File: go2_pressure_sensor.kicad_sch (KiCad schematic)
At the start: 11 parts, among them J1 Conn_01x03_Socket, U2 LP2980-ADJ

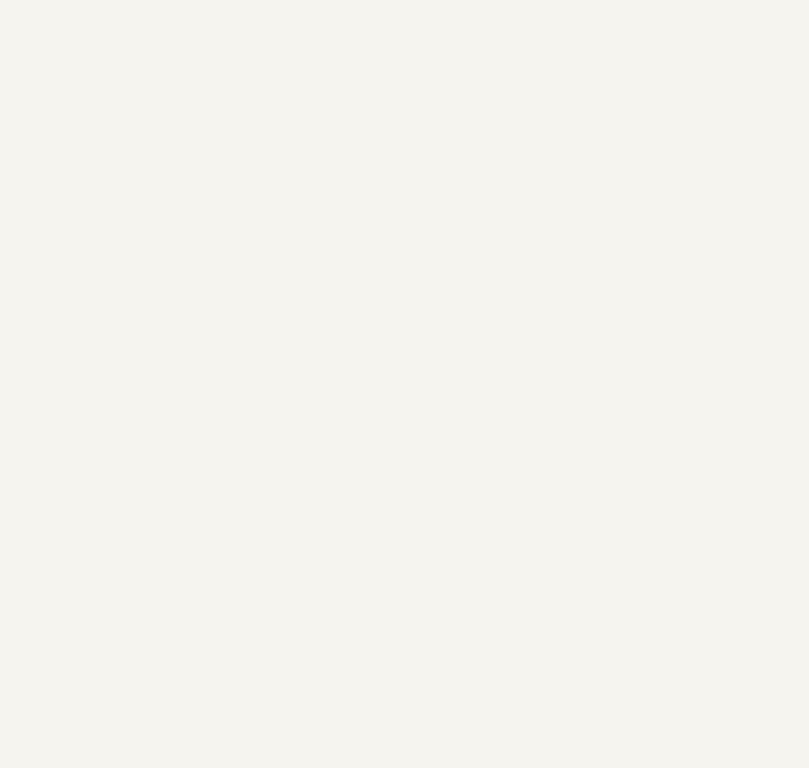
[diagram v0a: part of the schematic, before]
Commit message: Added connector diagram of the GO2 battery (unrelated)
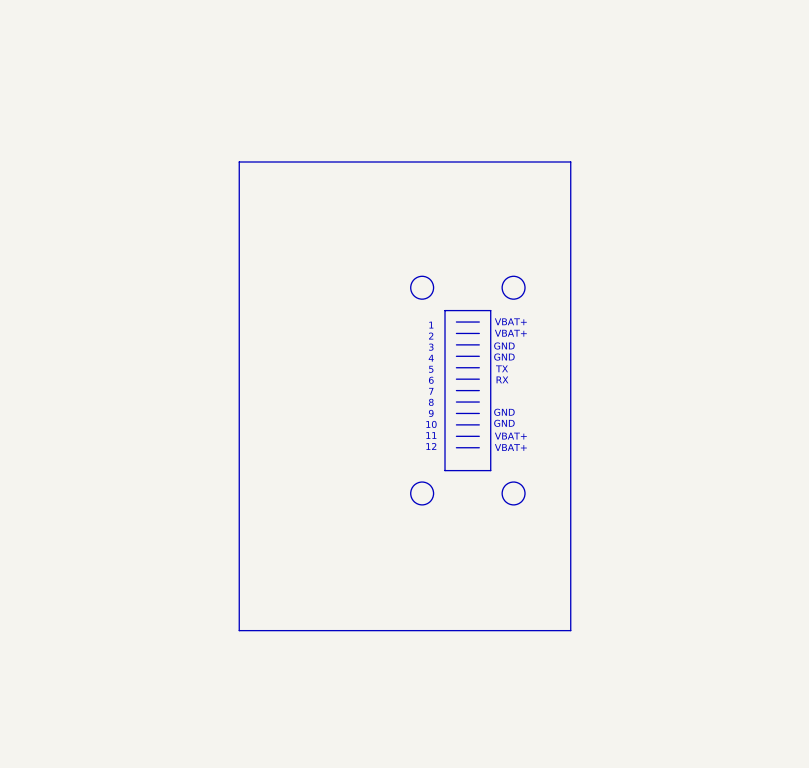
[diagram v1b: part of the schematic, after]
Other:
- note added: "1 2 3 4 5 6 7 8 9 10 11 12"
- note added: "GND GND"
- note added: "TX RX"
- note added: "VBAT+"

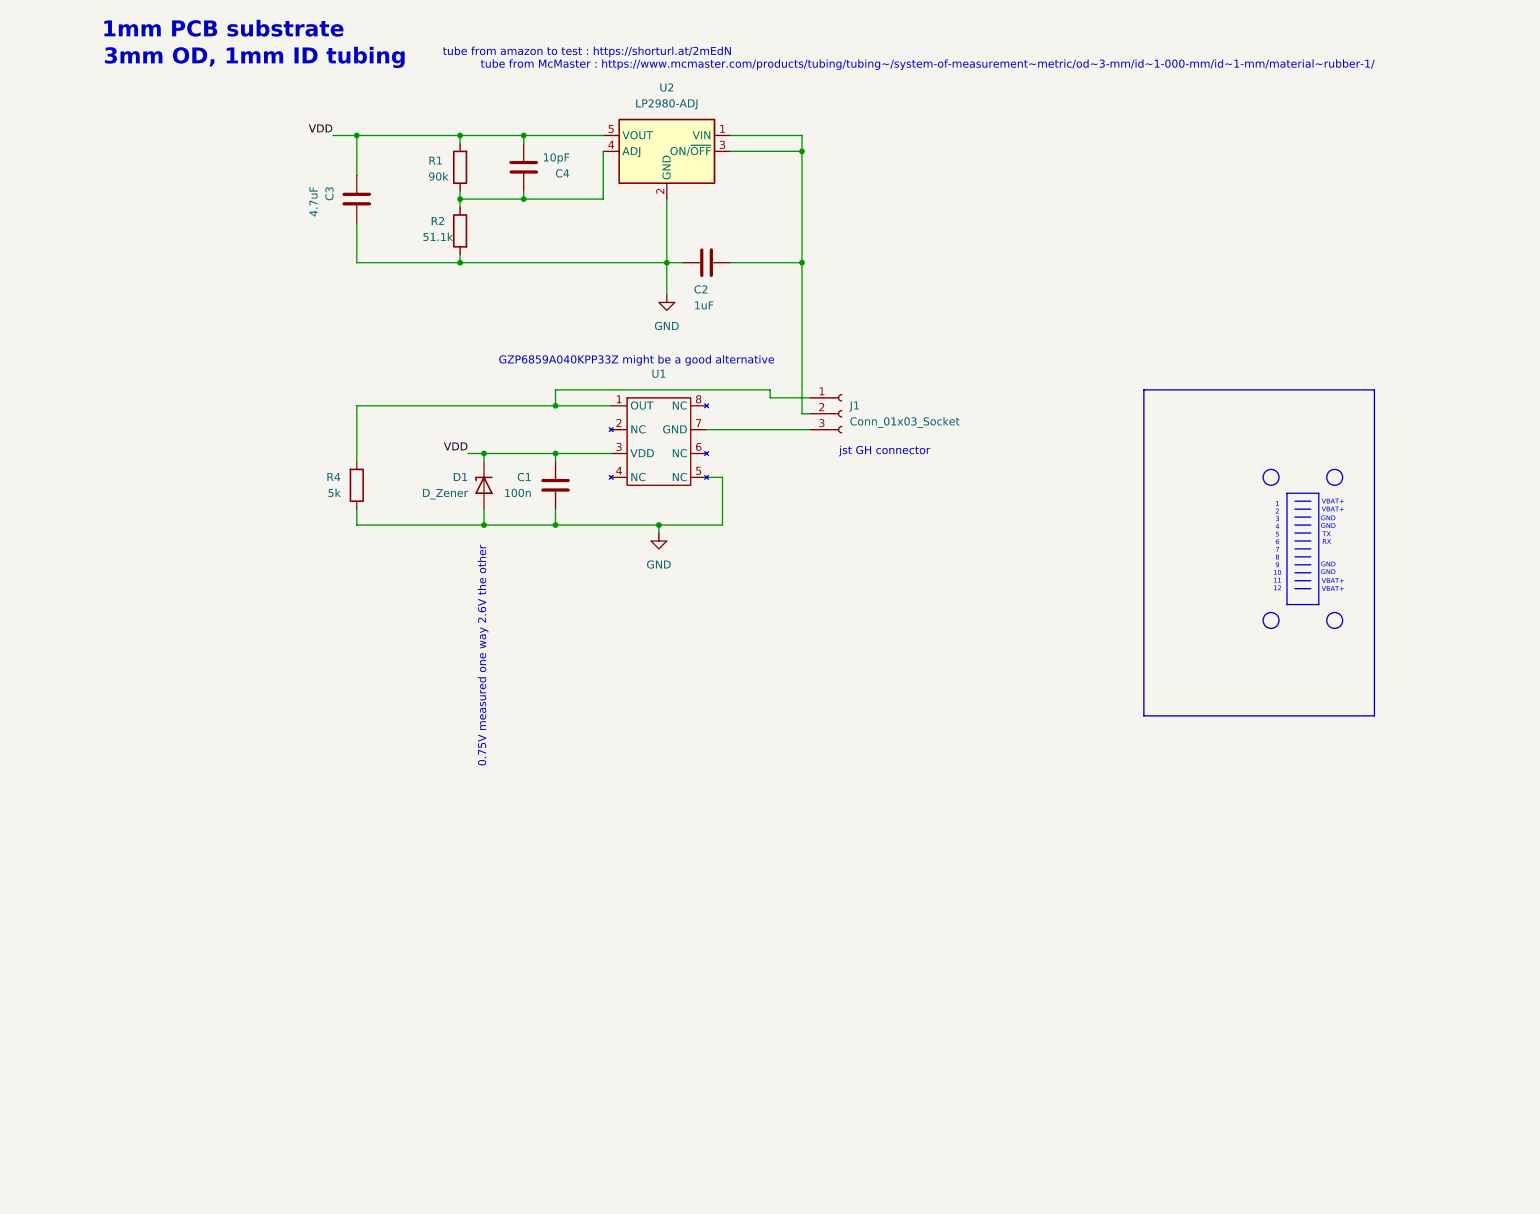
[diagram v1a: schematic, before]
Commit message: Non verified version with new presure transducer
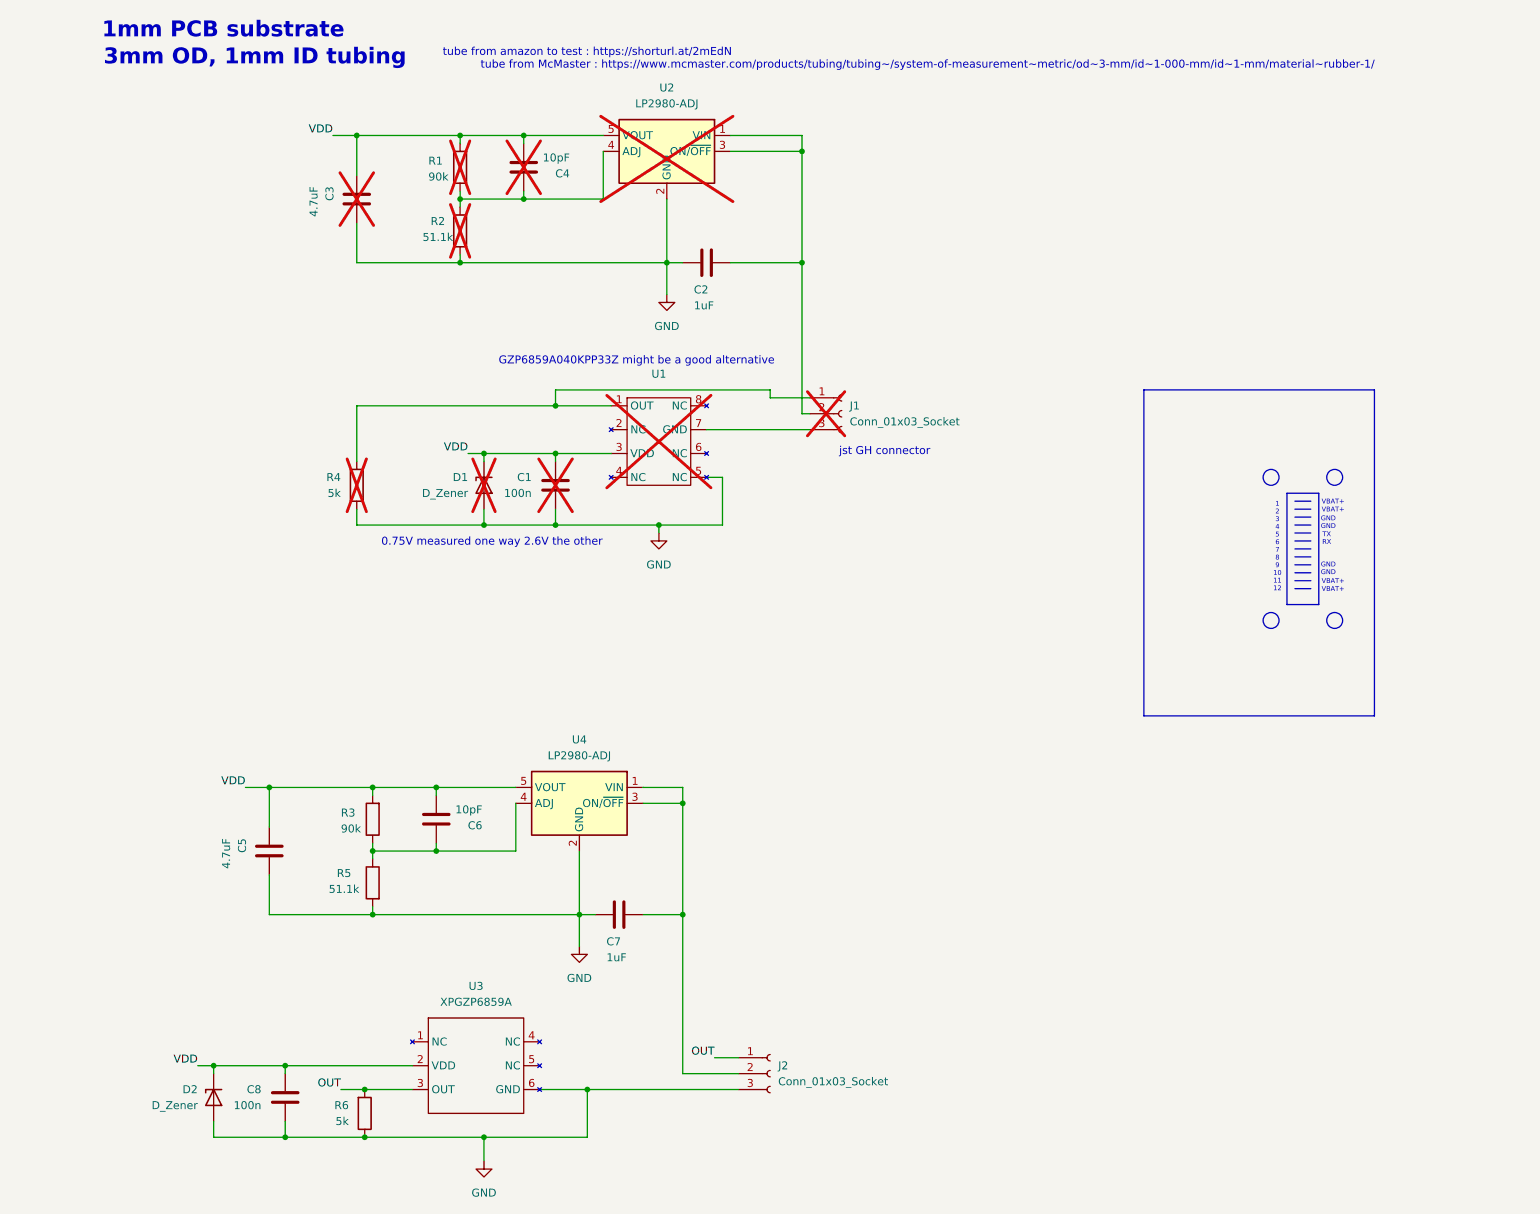
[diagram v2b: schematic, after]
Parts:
- added C5: 4.7uF, Resistor_SMD:R_0603_1608Metric, symbol Device:C
- added C6: 10pF, Resistor_SMD:R_0603_1608Metric, symbol Device:C
- added C7: 1uF, Resistor_SMD:R_0603_1608Metric, symbol Device:C
- added C8: 100n, Resistor_SMD:R_0603_1608Metric, symbol Device:C
- added D2: D_Zener, Diode_SMD:D_0603_1608Metric, symbol Device:D_Zener
- added J2: Conn_01x03_Socket, Connector_JST:JST_GH_BM03B-GHS-TBT_1x03-1MP_P1.25mm_Vertical, symbol Connector:Conn_01x03_Socket
- added R3: 90k, Resistor_SMD:R_0603_1608Metric, symbol Device:R
- added R5: 51.1k, Resistor_SMD:R_0603_1608Metric, symbol Device:R
- added R6: 5k, Resistor_SMD:R_0603_1608Metric, symbol Device:R
- added U3: XPGZP6859A, Ensmasteel_librairy:XGZ6859 6pin, symbol ENSMASTEEL_librairy:XPGZP6859A
- added U4: LP2980-ADJ, Package_TO_SOT_SMD:SOT-23-5, symbol Regulator_Linear:LP2980-ADJ
- C1, C3, C4, D1, J1, R1, R2, R4, U1, U2: now not fitted; now left out of the parts list
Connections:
- net GND: now also C5.1, C7.2, C8.2, D2.2 (A), J2.3 (Pin_3), R5.2, R6.1, U3.6 (GND), U4.2 (GND)
- net VDD: now also C5.2, C6.1, C8.1, D2.1 (K), R3.2, U3.2 (VDD), U4.5 (VOUT)
- new net: C6.2, R3.1, R5.1, U4.4 (ADJ)
- new net: C7.1, J2.2 (Pin_2), U4.1 (VIN), U4.3 (ON/~{OFF})
- new net OUT: J2.1 (Pin_1), R6.2, U3.3 (OUT)

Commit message: Removed copied sensors schematic
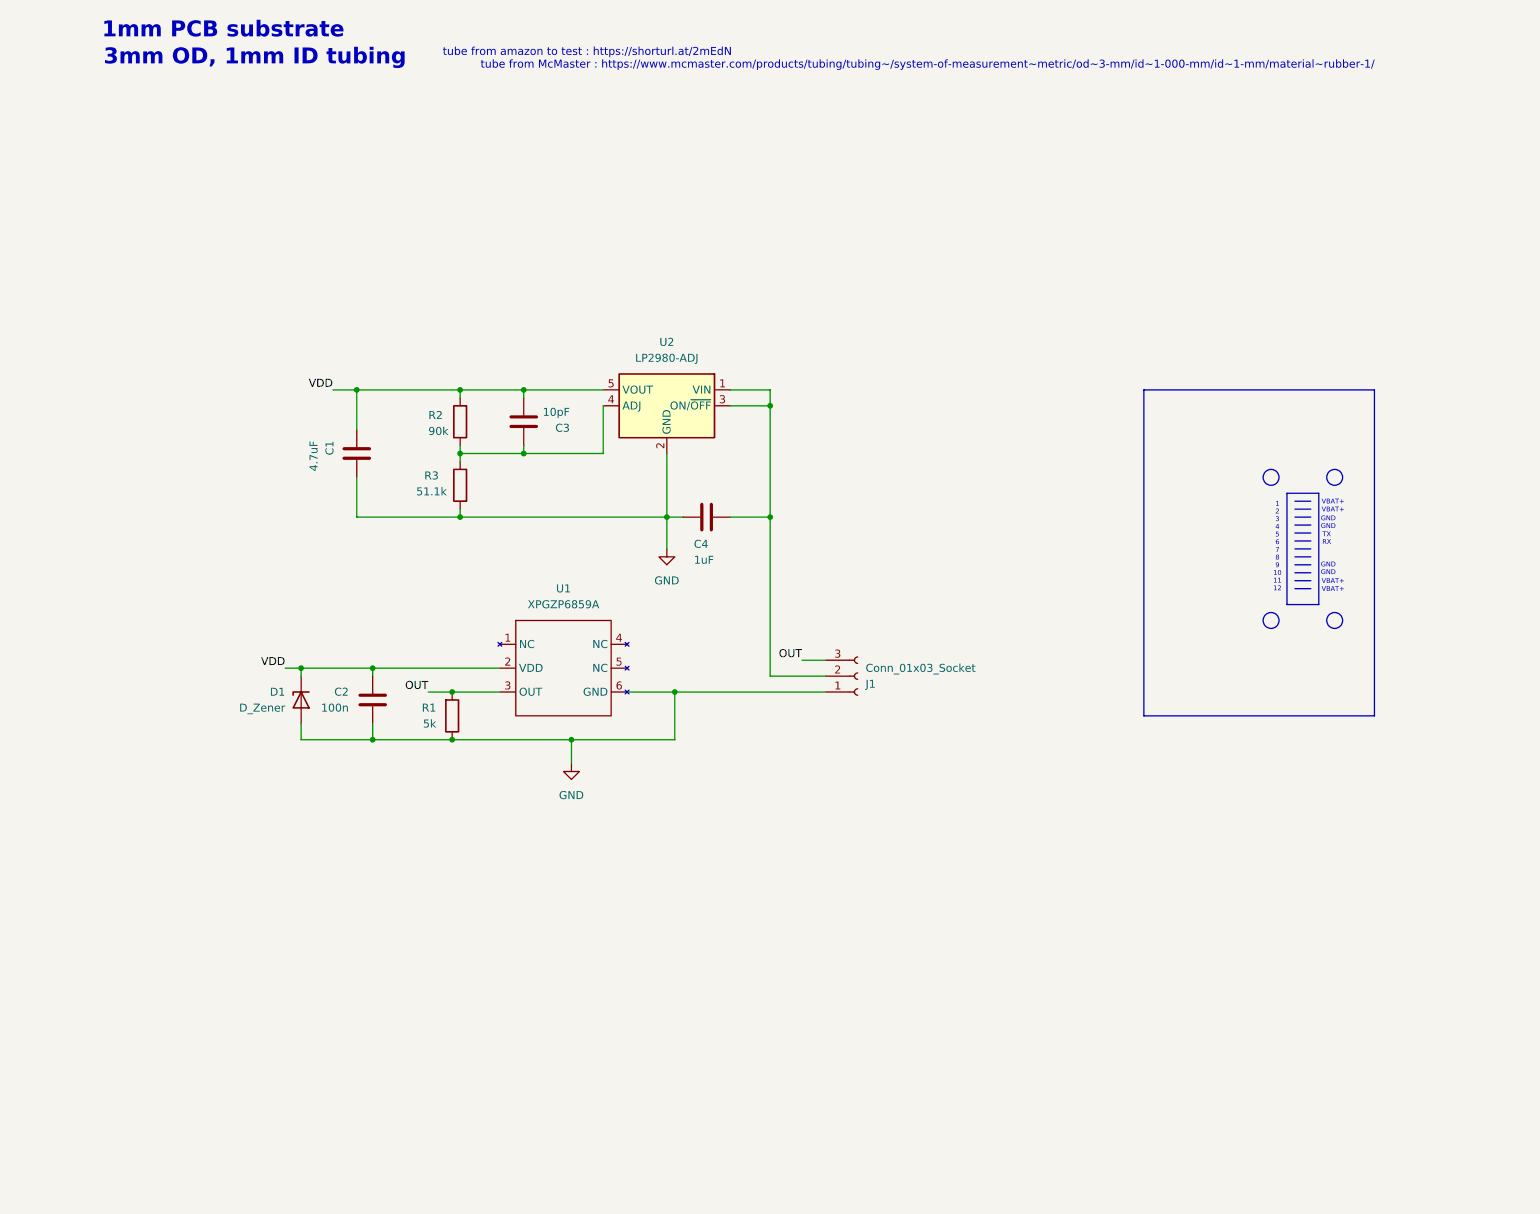
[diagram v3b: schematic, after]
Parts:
- removed C1: 100n, symbol Device:C
- removed C2: 1uF, symbol Device:C
- removed C3: 4.7uF, symbol Device:C
- removed C4: 10pF, symbol Device:C
- removed D1: D_Zener, symbol Device:D_Zener
- removed J1: Conn_01x03_Socket, symbol Connector:Conn_01x03_Socket
- removed R1: 90k, symbol Device:R
- removed R2: 51.1k, symbol Device:R
- removed R4: 5k, symbol Device:R
- removed U1: ~, symbol ENSMASTEEL_librairy:XGZP6869D
- removed U2: LP2980-ADJ, Package_TO_SOT_SMD:SOT-23-5, symbol Regulator_Linear:LP2980-ADJ
- C1: renamed from C5; LCSC (none) -> C19666
- C2: renamed from C8; footprint Resistor_SMD:R_0603_1608Metric -> Capacitor_SMD:C_0603_1608Metric; LCSC (none) -> C66501
- C3: renamed from C6; LCSC (none) -> C106245
- C4: renamed from C7; LCSC (none) -> C6119849
- D1: renamed from D2; footprint Diode_SMD:D_0603_1608Metric -> Diode_SMD:D_SOD-123; LCSC (none) -> C2117
- J1: renamed from J2; LCSC (none) -> C161691
- R1: renamed from R6; LCSC (none) -> C2828621
- R2: renamed from R3; LCSC (none) -> C23129
- R3: renamed from R5; LCSC (none) -> C2933234
- U1: renamed from U3; LCSC (none) -> C3038019
- U2: renamed from U4; LCSC (none) -> C5310801
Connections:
- net GND: now also J1.1 (Pin_1); no longer J1.3 (Pin_3)
- net OUT: now also J1.3 (Pin_3); no longer J1.1 (Pin_1)
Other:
- note removed: "0.75V measured one way 2.6V the other"
- note removed: "GZP6859A040KPP33Z might be a good alternative"
- note removed: "jst GH connector"
- moved on the sheet: C1, C2, C3, C4, D1, J1, R1, R2, R3, U1, U2
